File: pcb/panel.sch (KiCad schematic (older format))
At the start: 28 parts, among them IC1 ATMEGA168-20PU, P1 CONN_6, P2 I2C, P3 CONN_1, P4 CONN_1, P5 CONN_1, P6 CONN_1, P7 CONN_2, SW1 PUSHPUTTON, SW2 PUSHPUTTON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

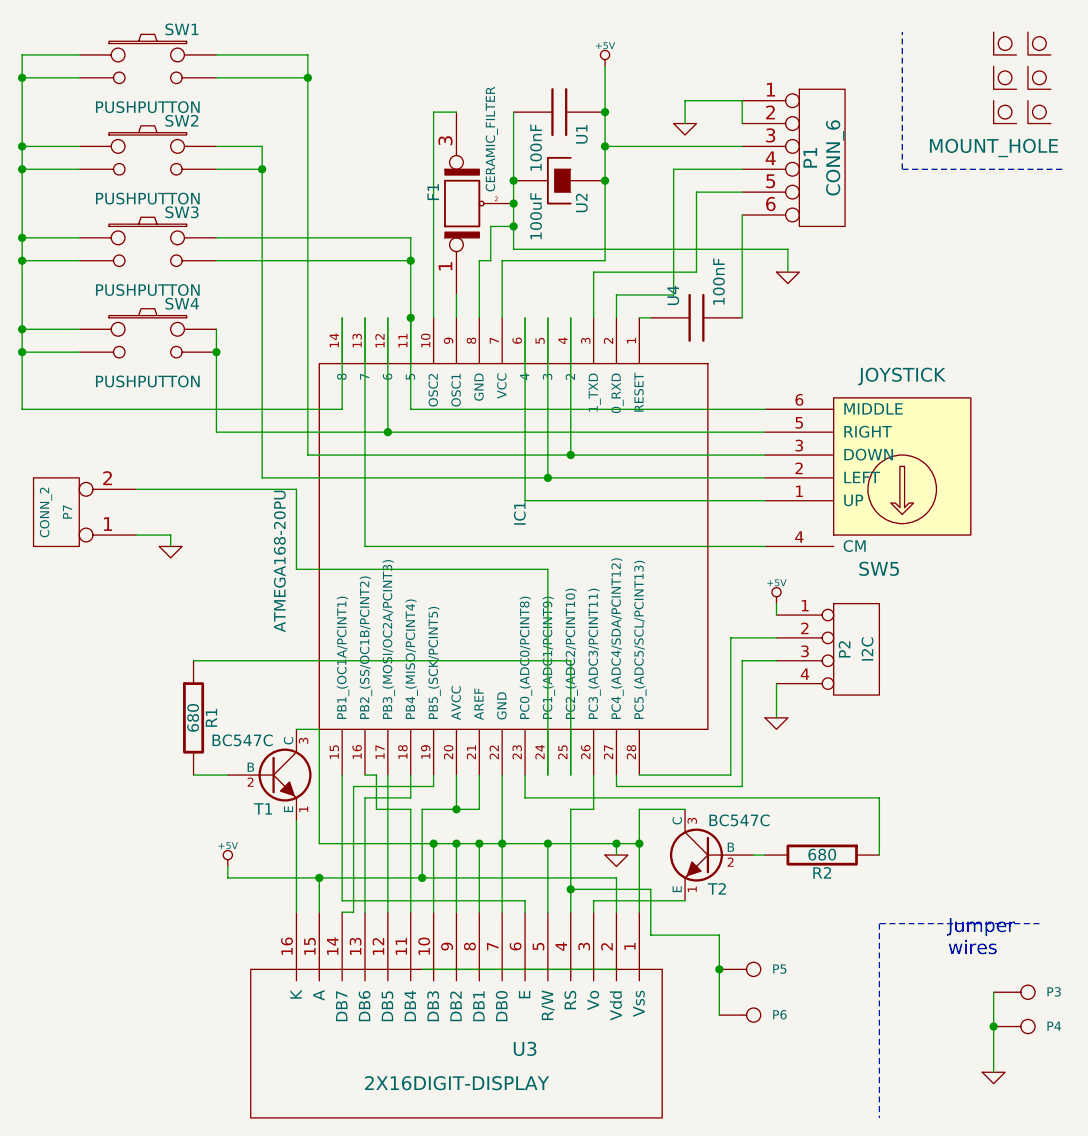
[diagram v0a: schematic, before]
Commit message: some changes made after testing with the first prototype. most important: switching contrast+lcd light to pwm pins
==> this version was prototyped and tested before this commit!
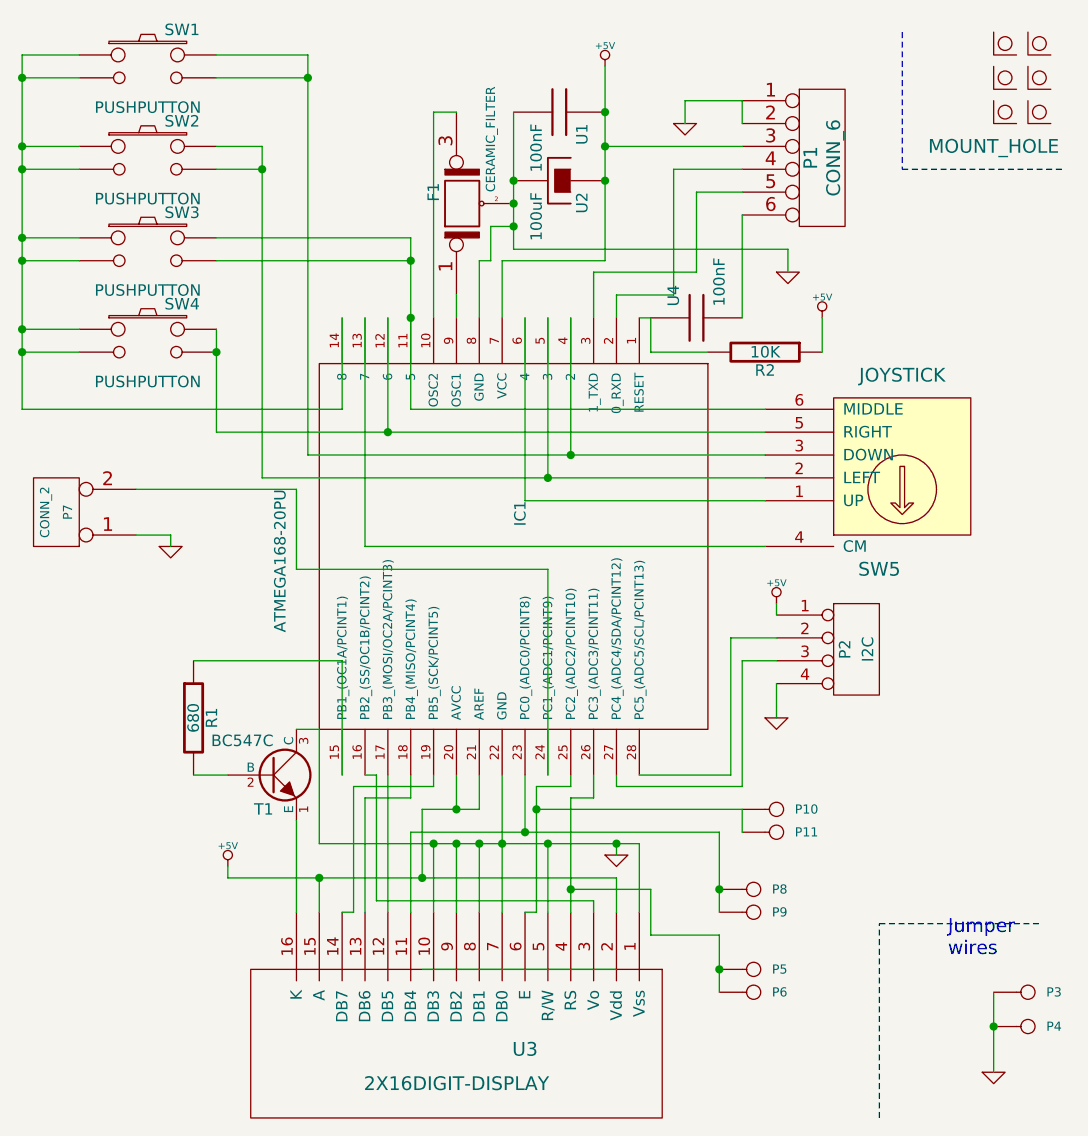
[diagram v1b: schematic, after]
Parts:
- removed T2: BC547C, symbol NPN
- added P10, P11, P8, P9: CONN_1, symbol CONN_1
- R2: value 680 -> 10K
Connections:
- net +5V: now also R2.1
- net at IC1.1 (RESET), U4.1: now also R2.2
- net at IC1.15 (PB1_(OC1A/PCINT1)): now also R1.1; no longer U3.6 (E)
- net at IC1.16 (PB2_(SS/OC1B/PCINT2)): now also U3.3 (Vo); no longer U3.11 (DB4)
- net at IC1.23 (PC0_(ADC0/PCINT8)): now also U3.11 (DB4), P8.1, P9.1; no longer R2.1
- net at IC1.25 (PC2_(ADC2/PCINT10)): now also U3.6 (E), P10.1, P11.1; no longer R1.1
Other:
- moved on the sheet: P6
